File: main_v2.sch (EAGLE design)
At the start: 33 parts, among them IC1 MAX6921, IC2 MAX6921, IC3 MC33063, IC4 LD33V05T, IC5 TDA7052A

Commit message: Pracical modifications
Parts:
- removed SJ1, SJ3, SJ4, SJ6: (no value), jumper:SJ
- removed SJ2: (no value), jumper:SJ2W
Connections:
- removed net HT+1: H1.1, H2.1, SJ2.3, SJ3.2
- removed net HT+4: H3.1, H4.1, SJ3.1
- removed net HT-1: H1.2, SJ2.1, SJ4.2
- removed net HT-2: H2.2, SJ1.1, SJ4.1
- removed net HT-3: H3.2, SJ1.2, SJ6.2
- removed net HT-4: H4.2, R11.1, SJ6.1
- new net HT+: H1.1, H2.1, H3.1, H4.1, R11.1
- new net HT-: H1.2, H2.2, H3.2, H4.2, R12.1
- new net N$14: IC1.OUT18
- new net N$15: IC1.OUT17
- new net N$16: IC1.OUT16
- new net N$17: IC1.OUT15
- new net N$18: IC1.OUT14
- new net N$19: IC1.OUT13
- new net N$20: IC1.OUT12
- new net N$21: IC1.OUT11
- new net N$22: IC1.OUT10
- new net N$23: IC1.OUT9
- new net N$24: IC1.OUT8
- new net N$25: IC1.OUT7
- new net N$26: IC1.OUT6
- new net N$27: IC1.OUT5
- new net N$28: IC1.OUT4
- new net N$29: IC1.OUT3
- new net N$30: IC1.OUT2
- new net N$31: IC1.OUT1
- new net N$32: IC1.OUT0
- new net N$33: IC2.OUT0
- new net N$34: IC2.OUT1
- new net N$35: IC2.OUT2
- new net N$36: IC2.OUT3
- new net N$37: IC2.OUT4
- new net N$38: IC2.OUT5
- new net N$39: IC2.OUT6
- new net N$40: IC2.OUT7
- new net N$41: IC2.OUT8
- new net N$42: IC2.OUT9
- new net N$43: IC2.OUT10
- new net N$44: IC2.OUT11
- new net N$45: IC2.OUT12
- new net N$46: IC2.OUT13
- new net N$47: IC2.OUT14
- new net N$48: IC2.OUT15
- new net N$49: IC2.OUT16
- new net N$50: IC2.OUT17
- new net N$51: IC2.OUT18
- new net N$52: IC2.OUT19
- net N$13: now also IC1.OUT19; no longer R12.1, SJ2.2

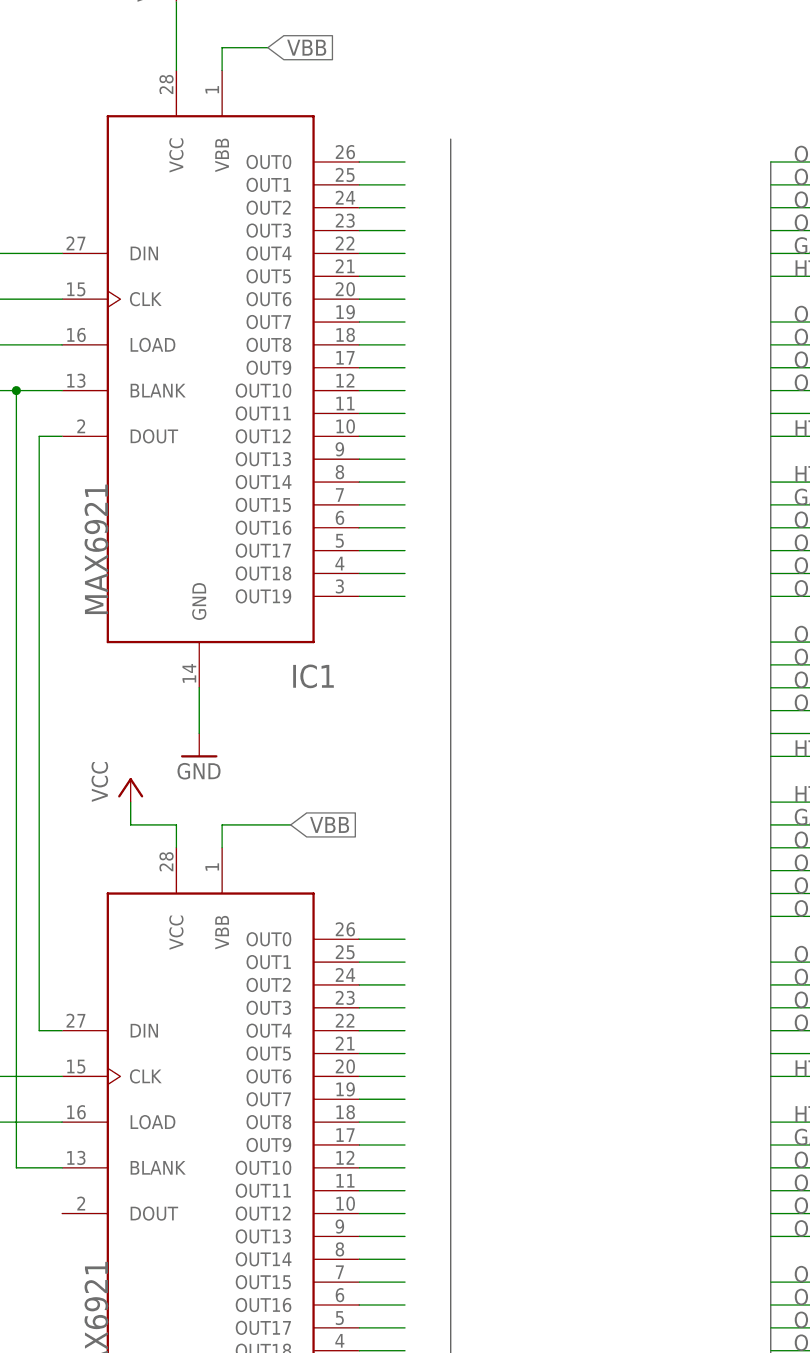
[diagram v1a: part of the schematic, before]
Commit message: Try wiring a few routes
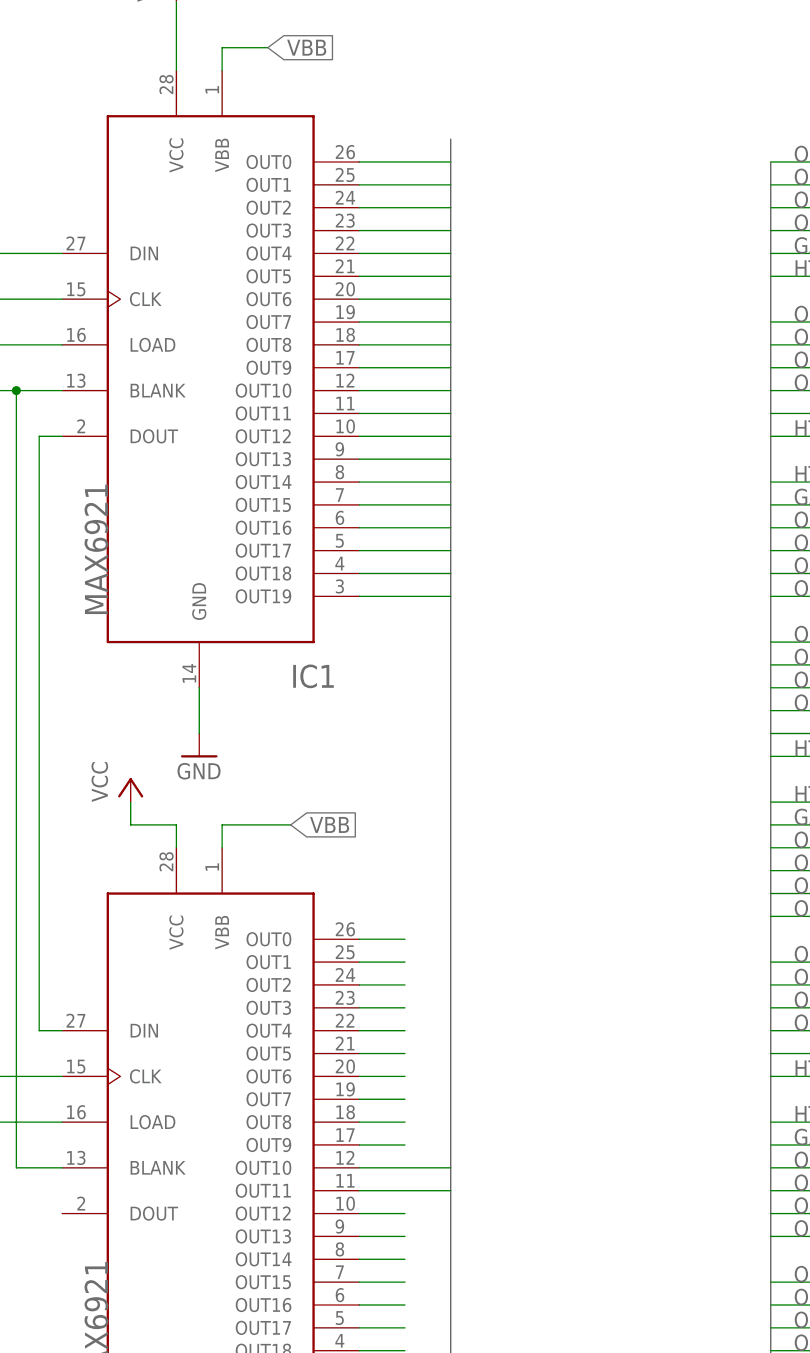
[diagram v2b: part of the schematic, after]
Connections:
- removed net N$13: IC1.OUT19
- removed net N$14: IC1.OUT18
- removed net N$15: IC1.OUT17
- removed net N$16: IC1.OUT16
- removed net N$17: IC1.OUT15
- removed net N$18: IC1.OUT14
- removed net N$19: IC1.OUT13
- removed net N$20: IC1.OUT12
- removed net N$21: IC1.OUT11
- removed net N$22: IC1.OUT10
- removed net N$23: IC1.OUT9
- removed net N$24: IC1.OUT8
- removed net N$25: IC1.OUT7
- removed net N$26: IC1.OUT6
- removed net N$27: IC1.OUT5
- removed net N$28: IC1.OUT4
- removed net N$29: IC1.OUT3
- removed net N$30: IC1.OUT2
- removed net N$31: IC1.OUT1
- removed net N$32: IC1.OUT0
- removed net N$43: IC2.OUT10
- removed net N$44: IC2.OUT11
- net GATE1: now also IC2.OUT10
- net GATE3: now also IC1.OUT10
- net GATE4: now also IC1.OUT9
- net OUT16: now also IC1.OUT11
- net OUT17: now also IC1.OUT12
- net OUT18: now also IC1.OUT13
- net OUT19: now also IC1.OUT14
- net OUT20: now also IC1.OUT15
- net OUT21: now also IC1.OUT16
- net OUT22: now also IC1.OUT17
- net OUT23: now also IC1.OUT18
- net OUT24: now also IC1.OUT0
- net OUT25: now also IC1.OUT1
- net OUT26: now also IC1.OUT2
- net OUT27: now also IC1.OUT3
- net OUT28: now also IC1.OUT4
- net OUT29: now also IC1.OUT5
- net OUT3: now also IC2.OUT11
- net OUT30: now also IC1.OUT6
- net OUT31: now also IC1.OUT7
- net SPARE3: now also IC1.OUT19
- net SPARE4: now also IC1.OUT8

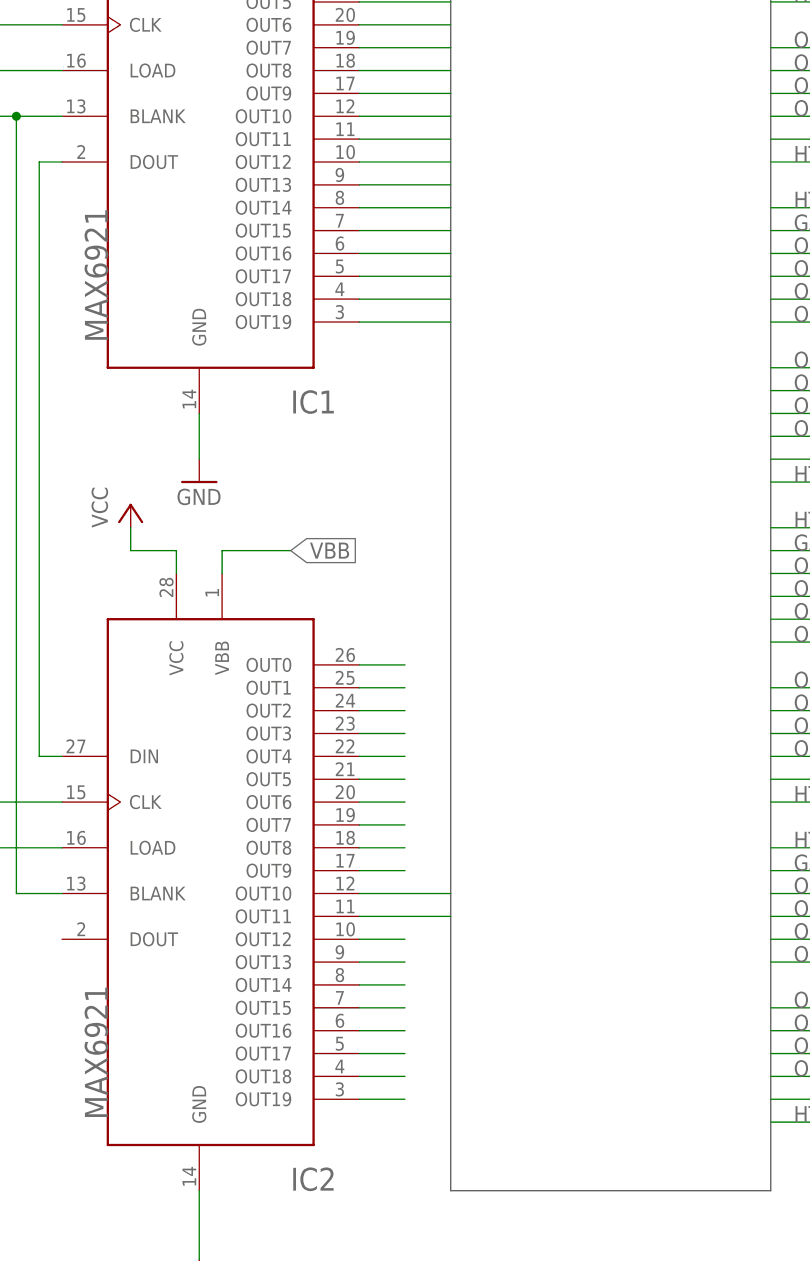
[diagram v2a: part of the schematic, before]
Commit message: Wire most of the board
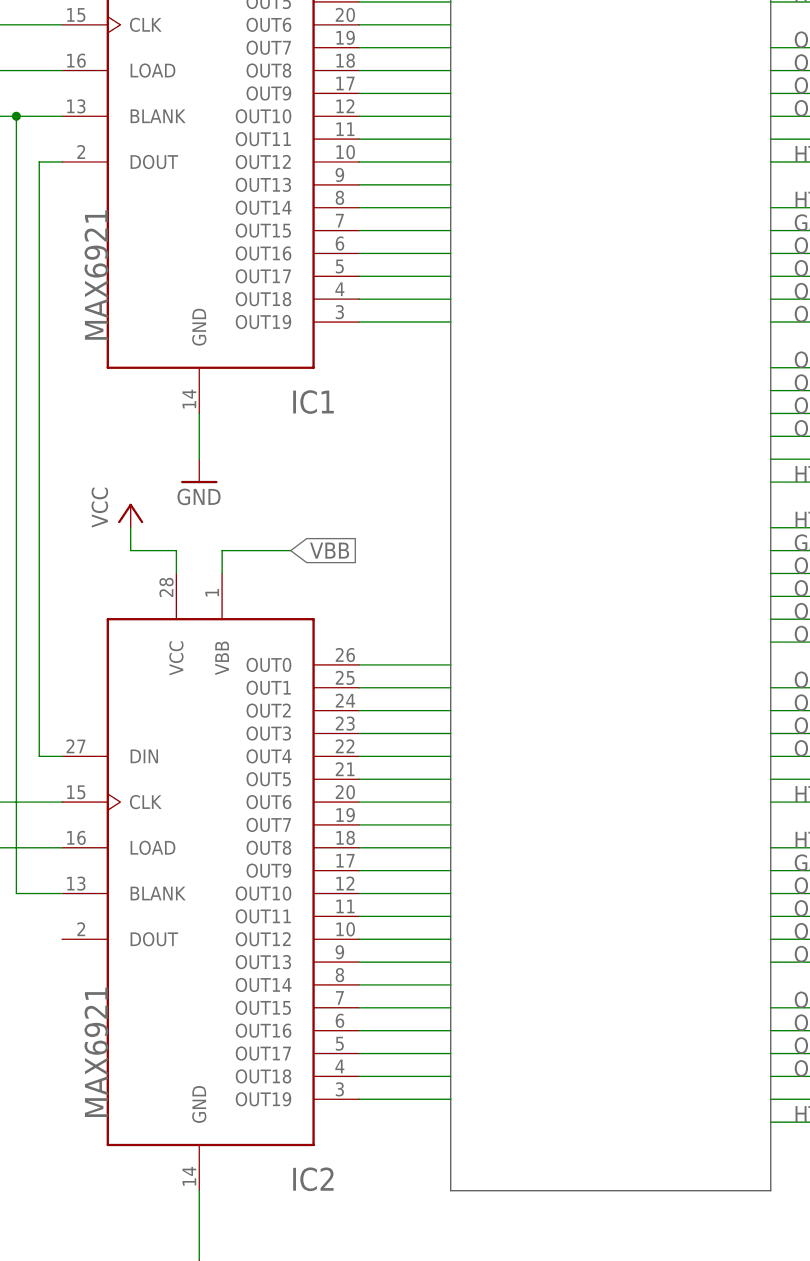
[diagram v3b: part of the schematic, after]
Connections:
- removed net N$33: IC2.OUT0
- removed net N$34: IC2.OUT1
- removed net N$35: IC2.OUT2
- removed net N$36: IC2.OUT3
- removed net N$37: IC2.OUT4
- removed net N$38: IC2.OUT5
- removed net N$39: IC2.OUT6
- removed net N$40: IC2.OUT7
- removed net N$41: IC2.OUT8
- removed net N$42: IC2.OUT9
- removed net N$45: IC2.OUT12
- removed net N$46: IC2.OUT13
- removed net N$47: IC2.OUT14
- removed net N$48: IC2.OUT15
- removed net N$49: IC2.OUT16
- removed net N$50: IC2.OUT17
- removed net N$51: IC2.OUT18
- removed net N$52: IC2.OUT19
- net GATE2: now also IC2.OUT8
- net OUT0: now also IC2.OUT12
- net OUT1: now also IC2.OUT15
- net OUT10: now also IC2.OUT1
- net OUT11: now also IC2.OUT7
- net OUT12: now also IC2.OUT6
- net OUT13: now also IC2.OUT0
- net OUT14: now also IC2.OUT2
- net OUT15: now also IC2.OUT4
- net OUT17: now also IC1.OUT14; no longer IC1.OUT12
- net OUT19: now also IC1.OUT12; no longer IC1.OUT14
- net OUT2: now also IC2.OUT17
- net OUT23: now also IC1.OUT19; no longer IC1.OUT18
- net OUT4: now also IC2.OUT13
- net OUT5: now also IC2.OUT14
- net OUT6: now also IC2.OUT16
- net OUT7: now also IC2.OUT19
- net OUT8: now also IC2.OUT5
- net OUT9: now also IC2.OUT3
- net SPARE1: now also IC2.OUT18
- net SPARE2: now also IC2.OUT9
- net SPARE3: now also IC1.OUT18; no longer IC1.OUT19
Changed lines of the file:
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@@
 <label x="195.58" y="160.02" size="1.778" layer="95"/>
+</segment>
+<segment>
+<pinref part="IC2" gate="G$1" pin="OUT12"/>
+<wire x1="157.48" y1="43.18" x2="147.32" y2="43.18" width="0.1524" layer="91"/>
 </segment>
 </net>
@@
 <label x="195.58" y="157.48" size="1.778" layer="95"/>
 </segment>
+<segment>
+<pinref part="IC2" gate="G$1" pin="OUT15"/>
+<wire x1="157.48" y1="35.56" x2="147.32" y2="35.56" width="0.1524" layer="91"/>
+</segment>
 </net>
 <net name="OUT2" class="0">
@@
 <label x="195.58" y="154.94" size="1.778" layer="95"/>
 </segment>
+<segment>
+<pinref part="IC2" gate="G$1" pin="OUT17"/>
+<wire x1="157.48" y1="30.48" x2="147.32" y2="30.48" width="0.1524" layer="91"/>
+</segment>
 </net>
 <net name="OUT3" class="0">
@@
 <label x="195.58" y="142.24" size="1.778" layer="95"/>
 </segment>
+<segment>
+<pinref part="IC2" gate="G$1" pin="OUT13"/>
+<wire x1="157.48" y1="40.64" x2="147.32" y2="40.64" width="0.1524" layer="91"/>
+</segment>
 </net>
 <net name="OUT5" class="0">
@@
 <label x="195.58" y="139.7" size="1.778" layer="95"/>
 </segment>
+<segment>
+<pinref part="IC2" gate="G$1" pin="OUT14"/>
+<wire x1="157.48" y1="38.1" x2="147.32" y2="38.1" width="0.1524" layer="91"/>
+</segment>
 </net>
 <net name="OUT6" class="0">
@@
 <label x="195.58" y="137.16" size="1.778" layer="95"/>
 </segment>
+<segment>
+<pinref part="IC2" gate="G$1" pin="OUT16"/>
+<wire x1="157.48" y1="33.02" x2="147.32" y2="33.02" width="0.1524" layer="91"/>
+</segment>
 </net>
 <net name="OUT7" class="0">
@@
 <wire x1="193.04" y1="134.62" x2="203.2" y2="134.62" width="0.1524" layer="91"/>
 <label x="195.58" y="134.62" size="1.778" layer="95"/>
+</segment>
+<segment>
+<pinref part="IC2" gate="G$1" pin="OUT19"/>
+<wire x1="157.48" y1="25.4" x2="147.32" y2="25.4" width="0.1524" layer="91"/>
 </segment>
 </net>
@@
 <label x="195.58" y="119.38" size="1.778" layer="95"/>
 </segment>
+<segment>
+<pinref part="IC2" gate="G$1" pin="OUT5"/>
+<wire x1="157.48" y1="60.96" x2="147.32" y2="60.96" width="0.1524" layer="91"/>
+</segment>
 </net>
 <net name="OUT9" class="0">
@@
 <label x="195.58" y="116.84" size="1.778" layer="95"/>
 </segment>
+<segment>
+<pinref part="IC2" gate="G$1" pin="OUT3"/>
+<wire x1="157.48" y1="66.04" x2="147.32" y2="66.04" width="0.1524" layer="91"/>
+</segment>
 </net>
 <net name="OUT10" class="0">
@@
 <label x="195.58" y="114.3" size="1.778" layer="95"/>
 </segment>
+<segment>
+<pinref part="IC2" gate="G$1" pin="OUT1"/>
+<wire x1="157.48" y1="71.12" x2="147.32" y2="71.12" width="0.1524" layer="91"/>
+</segment>
 </net>
 <net name="OUT11" class="0">
@@
 <label x="195.58" y="111.76" size="1.778" layer="95"/>
 </segment>
+<segment>
+<pinref part="IC2" gate="G$1" pin="OUT7"/>
+<wire x1="157.48" y1="55.88" x2="147.32" y2="55.88" width="0.1524" layer="91"/>
+</segment>
 </net>
 <net name="OUT12" class="0">
@@
 <label x="195.58" y="106.68" size="1.778" layer="95"/>
 </segment>
+<segment>
+<pinref part="IC2" gate="G$1" pin="OUT6"/>
+<wire x1="157.48" y1="58.42" x2="147.32" y2="58.42" width="0.1524" layer="91"/>
+</segment>
 </net>
 <net name="OUT13" class="0">
@@
 <label x="195.58" y="104.14" size="1.778" layer="95"/>
 </segment>
+<segment>
+<pinref part="IC2" gate="G$1" pin="OUT0"/>
+<wire x1="157.48" y1="73.66" x2="147.32" y2="73.66" width="0.1524" layer="91"/>
+</segment>
 </net>
 <net name="OUT14" class="0">
@@
 <label x="195.58" y="101.6" size="1.778" layer="95"/>
 </segment>
+<segment>
+<pinref part="IC2" gate="G$1" pin="OUT2"/>
+<wire x1="157.48" y1="68.58" x2="147.32" y2="68.58" width="0.1524" layer="91"/>
+</segment>
 </net>
 <net name="OUT15" class="0">
@@
 <wire x1="193.04" y1="99.06" x2="203.2" y2="99.06" width="0.1524" layer="91"/>
 <label x="195.58" y="99.06" size="1.778" layer="95"/>
+</segment>
+<segment>
+<pinref part="IC2" gate="G$1" pin="OUT4"/>
+<wire x1="157.48" y1="63.5" x2="147.32" y2="63.5" width="0.1524" layer="91"/>
 </segment>
 </net>
@@
 </segment>
 <segment>
-<pinref part="IC1" gate="G$1" pin="OUT12"/>
-<wire x1="147.32" y1="129.54" x2="157.48" y2="129.54" width="0.1524" layer="91"/>
+<pinref part="IC1" gate="G$1" pin="OUT14"/>
+<wire x1="157.48" y1="124.46" x2="147.32" y2="124.46" width="0.1524" layer="91"/>
 </segment>
 </net>
@@
 </segment>
 <segment>
-<pinref part="IC1" gate="G$1" pin="OUT14"/>
-<wire x1="147.32" y1="124.46" x2="157.48" y2="124.46" width="0.1524" layer="91"/>
+<pinref part="IC1" gate="G$1" pin="OUT12"/>
+<wire x1="157.48" y1="129.54" x2="147.32" y2="129.54" width="0.1524" layer="91"/>
 </segment>
 </net>
@@
 </segment>
 <segment>
-<pinref part="IC1" gate="G$1" pin="OUT18"/>
-<wire x1="147.32" y1="114.3" x2="157.48" y2="114.3" width="0.1524" layer="91"/>
+<pinref part="IC1" gate="G$1" pin="OUT19"/>
+<wire x1="157.48" y1="111.76" x2="147.32" y2="111.76" width="0.1524" layer="91"/>
 </segment>
 </net>
@@
 <wire x1="228.6" y1="96.52" x2="218.44" y2="96.52" width="0.1524" layer="91"/>
 <label x="195.58" y="121.92" size="1.778" layer="95"/>
+</segment>
+<segment>
+<pinref part="IC2" gate="G$1" pin="OUT8"/>
+<wire x1="157.48" y1="53.34" x2="147.32" y2="53.34" width="0.1524" layer="91"/>
 </segment>
 </net>
@@
 <wire x1="203.2" y1="132.08" x2="193.04" y2="132.08" width="0.1524" layer="91"/>
 </segment>
+<segment>
+<pinref part="IC2" gate="G$1" pin="OUT18"/>
+<wire x1="157.48" y1="27.94" x2="147.32" y2="27.94" width="0.1524" layer="91"/>
+</segment>
 </net>
 <net name="SPARE2" class="0">
@@
 <wire x1="203.2" y1="96.52" x2="193.04" y2="96.52" width="0.1524" layer="91"/>
 </segment>
+<segment>
+<pinref part="IC2" gate="G$1" pin="OUT9"/>
+<wire x1="157.48" y1="50.8" x2="147.32" y2="50.8" width="0.1524" layer="91"/>
+</segment>
 </net>
 <net name="SPARE3" class="0">
@@
 </segment>
 <segment>
-<pinref part="IC1" gate="G$1" pin="OUT19"/>
-<wire x1="147.32" y1="111.76" x2="157.48" y2="111.76" width="0.1524" layer="91"/>
+<pinref part="IC1" gate="G$1" pin="OUT18"/>
+<wire x1="157.48" y1="114.3" x2="147.32" y2="114.3" width="0.1524" layer="91"/>
 </segment>
 </net>
@@
 </segment>
 </net>
-<net name="N$33" class="0">
-<segment>
-<pinref part="IC2" gate="G$1" pin="OUT0"/>
-<wire x1="147.32" y1="73.66" x2="152.4" y2="73.66" width="0.1524" layer="91"/>
-</segment>
-</net>
-<net name="N$34" class="0">
-<segment>
-<pinref part="IC2" gate="G$1" pin="OUT1"/>
-<wire x1="147.32" y1="71.12" x2="152.4" y2="71.12" width="0.1524" layer="91"/>
-</segment>
-</net>
-<net name="N$35" class="0">
-<segment>
-<pinref part="IC2" gate="G$1" pin="OUT2"/>
-<wire x1="147.32" y1="68.58" x2="152.4" y2="68.58" width="0.1524" layer="91"/>
-</segment>
-</net>
-<net name="N$36" class="0">
-<segment>
-<pinref part="IC2" gate="G$1" pin="OUT3"/>
-<wire x1="147.32" y1="66.04" x2="152.4" y2="66.04" width="0.1524" layer="91"/>
-</segment>
-</net>
-<net name="N$37" class="0">
-<segment>
-<pinref part="IC2" gate="G$1" pin="OUT4"/>
-<wire x1="147.32" y1="63.5" x2="152.4" y2="63.5" width="0.1524" layer="91"/>
-</segment>
-</net>
-<net name="N$38" class="0">
-<segment>
-<pinref part="IC2" gate="G$1" pin="OUT5"/>
-<wire x1="147.32" y1="60.96" x2="152.4" y2="60.96" width="0.1524" layer="91"/>
-</segment>
-</net>
-<net name="N$39" class="0">
-<segment>
-<pinref part="IC2" gate="G$1" pin="OUT6"/>
-<wire x1="147.32" y1="58.42" x2="152.4" y2="58.42" width="0.1524" layer="91"/>
-</segment>
-</net>
-<net name="N$40" class="0">
-<segment>
-<pinref part="IC2" gate="G$1" pin="OUT7"/>
-<wire x1="147.32" y1="55.88" x2="152.4" y2="55.88" width="0.1524" layer="91"/>
-</segment>
-</net>
-<net name="N$41" class="0">
-<segment>
-<pinref part="IC2" gate="G$1" pin="OUT8"/>
-<wire x1="147.32" y1="53.34" x2="152.4" y2="53.34" width="0.1524" layer="91"/>
-</segment>
-</net>
-<net name="N$42" class="0">
-<segment>
-<pinref part="IC2" gate="G$1" pin="OUT9"/>
-<wire x1="147.32" y1="50.8" x2="152.4" y2="50.8" width="0.1524" layer="91"/>
-</segment>
-</net>
-<net name="N$45" class="0">
-<segment>
-<pinref part="IC2" gate="G$1" pin="OUT12"/>
-<wire x1="147.32" y1="43.18" x2="152.4" y2="43.18" width="0.1524" layer="91"/>
-</segment>
-</net>
-<net name="N$46" class="0">
-<segment>
-<pinref part="IC2" gate="G$1" pin="OUT13"/>
-<wire x1="147.32" y1="40.64" x2="152.4" y2="40.64" width="0.1524" layer="91"/>
-</segment>
-</net>
-<net name="N$47" class="0">
-<segment>
-<pinref part="IC2" gate="G$1" pin="OUT14"/>
-<wire x1="147.32" y1="38.1" x2="152.4" y2="38.1" width="0.1524" layer="91"/>
-</segment>
-</net>
-<net name="N$48" class="0">
-<segment>
-<pinref part="IC2" gate="G$1" pin="OUT15"/>
-<wire x1="147.32" y1="35.56" x2="152.4" y2="35.56" width="0.1524" layer="91"/>
-</segment>
-</net>
-<net name="N$49" class="0">
-<segment>
-<pinref part="IC2" gate="G$1" pin="OUT16"/>
-<wire x1="147.32" y1="33.02" x2="152.4" y2="33.02" width="0.1524" layer="91"/>
-</segment>
-</net>
-<net name="N$50" class="0">
-<segment>
-<pinref part="IC2" gate="G$1" pin="OUT17"/>
-<wire x1="147.32" y1="30.48" x2="152.4" y2="30.48" width="0.1524" layer="91"/>
-</segment>
-</net>
-<net name="N$51" class="0">
-<segment>
-<pinref part="IC2" gate="G$1" pin="OUT18"/>
-<wire x1="147.32" y1="27.94" x2="152.4" y2="27.94" width="0.1524" layer="91"/>
-</segment>
-</net>
-<net name="N$52" class="0">
-<segment>
-<pinref part="IC2" gate="G$1" pin="OUT19"/>
-<wire x1="147.32" y1="25.4" x2="152.4" y2="25.4" width="0.1524" layer="91"/>
-</segment>
-</net>
